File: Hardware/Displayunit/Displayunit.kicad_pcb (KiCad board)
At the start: 2 copper layers, 99 parts, among them IC1 TSC2007, IC2 MX25LM51245GXDI00, IC3 IS66WVH8M8BLL-100B1LI_0, J1 USB_B_Micro, J2 8P8C_Shielded, J3 54104-4031, J4 Conn_ARM_JTAG_SWD_20, J5 52271-0679, J6 Conn_02x06_Odd_Even, Q1 2N7002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

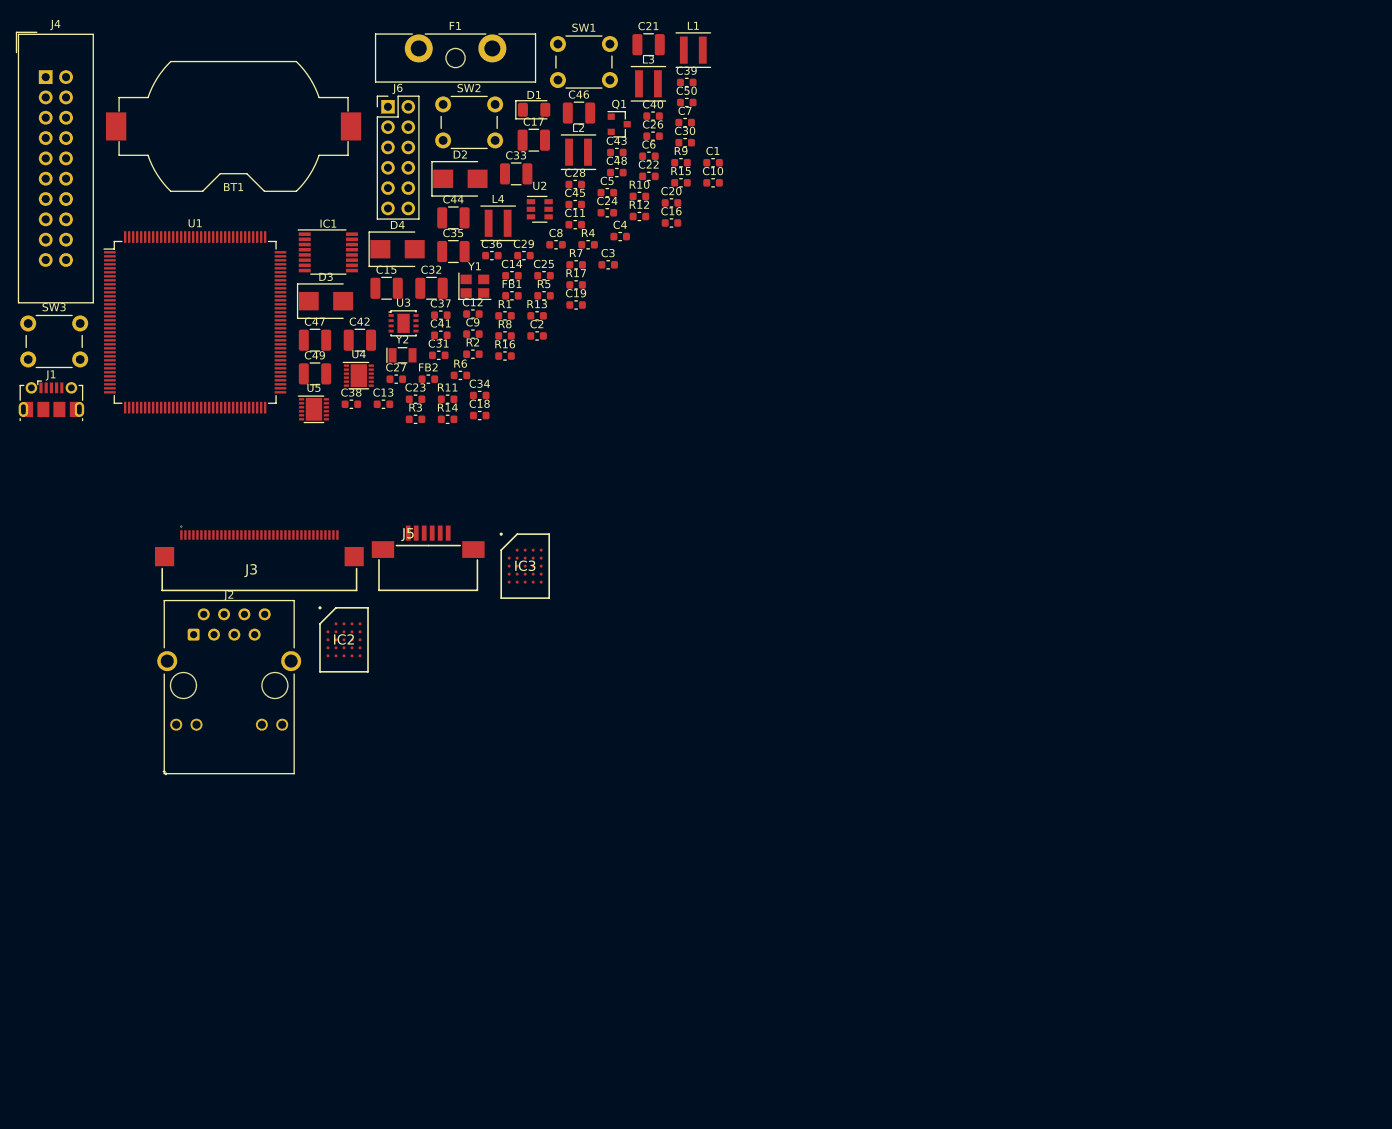
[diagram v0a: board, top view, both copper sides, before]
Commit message: Display Board kleinere Schaltplan Anpassung , Board Design an New Heaven Display angepasst, Platzierung zu 95 % abgeschlossen
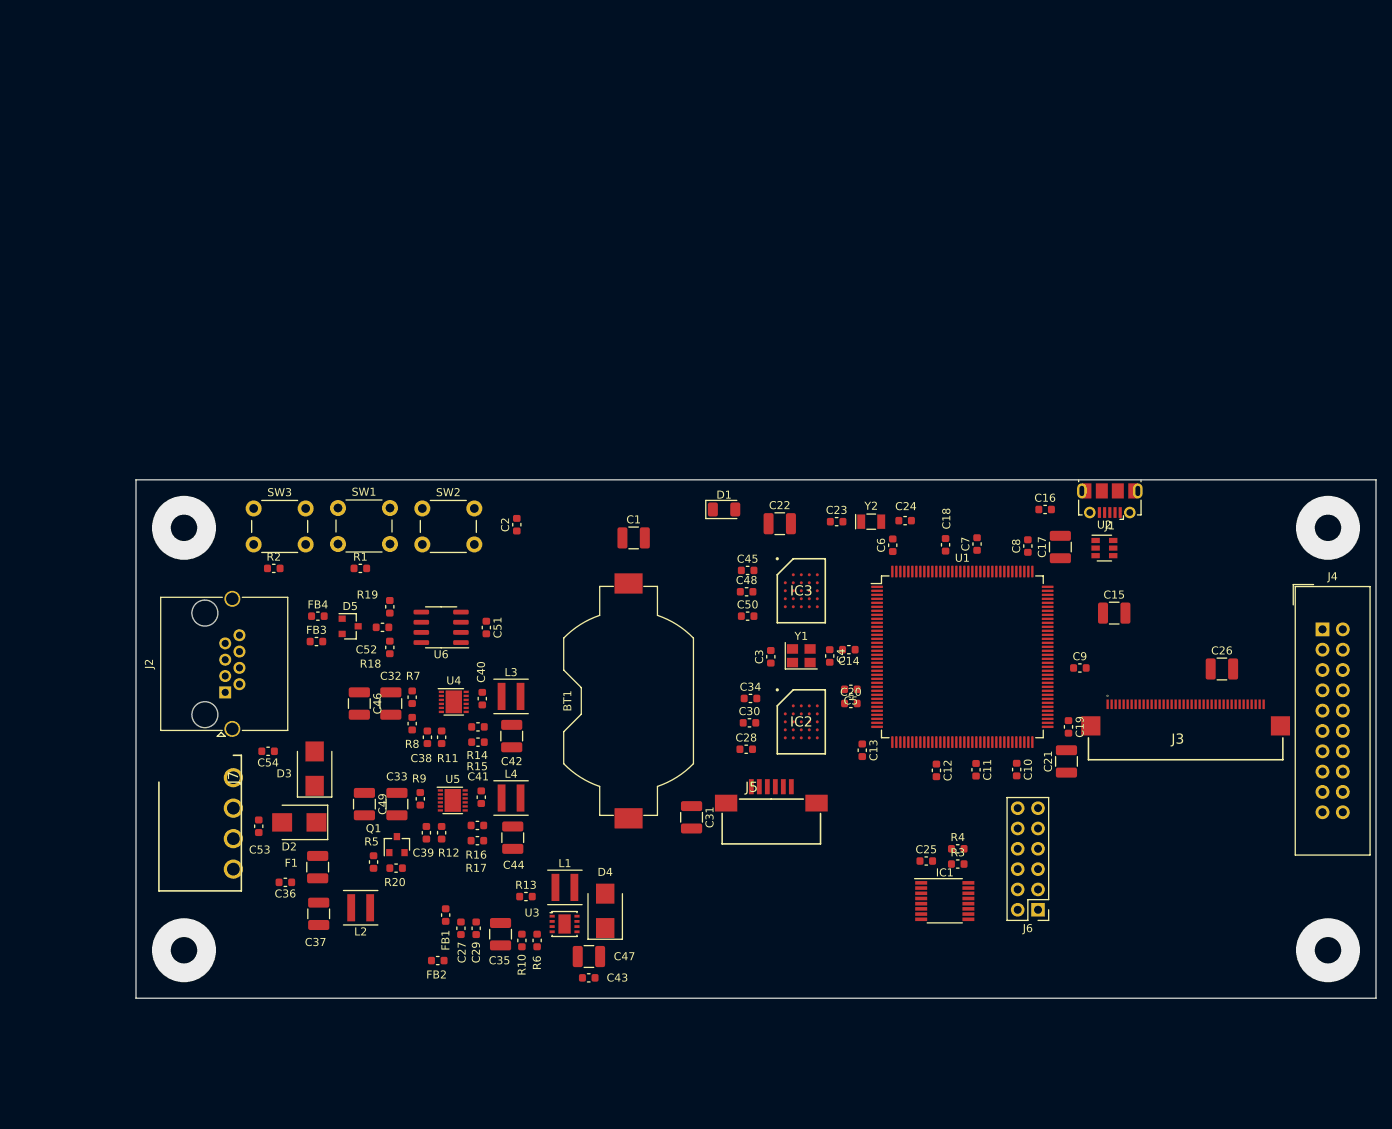
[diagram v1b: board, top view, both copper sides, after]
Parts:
- added C51: 100n, Capacitor_SMD:C_0603_1608Metric, F.Cu at (105.8, 67.5)
- added C52: 5n6, Capacitor_SMD:C_0603_1608Metric, F.Cu at (92.8, 67.4)
- added C53: 100n, Capacitor_SMD:C_0603_1608Metric, F.Cu at (77.3, 92.3)
- added C54: 100n, Capacitor_SMD:C_0603_1608Metric, F.Cu at (78.5, 82.9)
- added D5: NUP2105L, Package_TO_SOT_SMD:SOT-23, F.Cu at (88.8, 67.3)
- added FB3: 100R, Inductor_SMD:L_0603_1608Metric, F.Cu at (84.6, 69.2)
- added FB4: 100R, Inductor_SMD:L_0603_1608Metric, F.Cu at (84.7, 66.0)
- added J7: 734-264, WAGO:SHDR4W120P0X381_1X4_1640X1030X850P, F.Cu at (74.2, 86.2)
- added R18: 60R, Resistor_SMD:R_0603_1608Metric, F.Cu at (93.7, 70.0)
- added R19: 60R, Resistor_SMD:R_0603_1608Metric, F.Cu at (93.7, 64.9)
- added R20: 100k, Resistor_SMD:R_0603_1608Metric, F.Cu at (94.5, 97.5)
- added U6: SN65HVD231, Package_SO:SOIC-8_3.9x4.9mm_P1.27mm, F.Cu at (100.1, 67.4)
- C1, C22, C26, C31, C37: footprint Capacitor_SMD:C_0603_1608Metric -> Capacitor_SMD:C_1210_3225Metric
- D2, D3, D4: value B345BE-13 -> B250
- F1: value KFZ 5A -> PFUF.150.2 30V 1.5A; footprint Fuse:Fuseholder_Blade_ATO_Littelfuse_Pudenz_2_Pin -> Fuse:Fuse_1210_3225Metric
- J2: footprint Connector_RJ:RJ45_Hanrun_HR911105A -> Connector_RJ:RJ45_Amphenol_RJHSE5380
- moved J4 173.9 mm to (210.3, 67.7)
- moved J1 132.9 mm to (183.7, 51.6), turned to 180 degrees
- moved J6 129.1 mm to (174.8, 102.7), turned to 180 degrees
- moved J3 117.7 mm to (193.2, 77.4)
- moved IC1 111.9 mm to (163.1, 101.7)
- moved L1 105.9 mm to (115.6, 99.9)
- moved U1 104.6 mm to (165.3, 71.1)
- moved C21 103.7 mm to (178.3, 84.2), turned to 90 degrees
- moved C43 103.2 mm to (118.6, 111.3), turned to 180 degrees
- moved F1 103.1 mm to (84.7, 97.4), turned to 90 degrees
- moved C15 99.6 mm to (184.3, 65.7)
- moved C39 99.3 mm to (98.3, 93.1), turned to 270 degrees
- moved L2 98.3 mm to (90.1, 102.5), turned to 180 degrees
- moved C26 97.4 mm to (197.7, 72.6)
- moved Q1 94.2 mm to (94.6, 94.6), turned to 90 degrees
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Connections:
- C17 pad 2: GND1 -> GND
- C18 pad 1: GND1 -> GND
- C19 pad 1: GND1 -> GND
- C20 pad 1: GND1 -> GND
- C21 pad 1: GND1 -> GND
- C25 pad 2: VCC -> +3.3VA
- C26 pad 1: VCC -> +3.3VA
- C31 pad 1: VCC -> +3.3VA
- D2 pad 1: GND -> Net-(D2-Pad1)
- D2 pad 2: Net-(D2-Pad2) -> Net-(C53-Pad1)
- D3 pad 1: GND -> Net-(D2-Pad1)
- D3 pad 2: Net-(D2-Pad2) -> Control+
- D4 pad 1: Net-(D4-Pad1) -> LCD_LED-A
- D4 pad 2: LCD_LED-A -> Net-(D4-Pad2)
- F1 pad 1: Net-(D2-Pad2) -> Net-(C36-Pad1)
- F1 pad 2: Net-(C36-Pad1) -> Net-(D2-Pad1)
- FB1 pad 2: Net-(FB1-Pad2) -> +3.3VA
- IC1 pad 1: VCC -> +3.3VA
- IC1 pad 2: Net-(IC1-Pad2) -> X+
- IC1 pad 3: Net-(IC1-Pad3) -> Y+
- IC1 pad 4: Net-(IC1-Pad4) -> X-
- IC1 pad 5: Net-(IC1-Pad5) -> Y-
- IC2 pad B4: VCCQ -> +3V3
- IC2 pad D1: VCCQ -> +3V3
- IC3 pad B4: VCCQ -> +3V3
- IC3 pad D1: VCCQ -> +3V3
- J2 pad 1: Net-(J2-Pad1) -> Control+
- J2 pad 2: Net-(J2-Pad2) -> Control+
- J2 pad 7: Net-(J2-Pad7) -> GND
- J2 pad 8: Net-(J2-Pad8) -> GND
- J2 pad SH: Net-(J2-PadSH) -> GND
- J3 pad 4: VCC -> +3.3VA
- J5 pad 1: VCC -> +3.3VA
- J5 pad 2: Net-(J5-Pad2) -> GND
- L1 pad 2: Net-(D4-Pad1) -> Net-(D4-Pad2)
- L2 pad 2: Net-(D2-Pad2) -> Net-(C36-Pad1)
- R13 pad 1: +VSW -> +3.3VA
- R3 pad 1: VCC -> +3.3VA
- R4 pad 1: VCC -> +3.3VA
- U2 pad 3: Net-(U2-Pad3) -> USB_D+
- U3 pad 8: Net-(D4-Pad1) -> Net-(D4-Pad2)
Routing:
- net GND: vias 0 -> 1
- net (no net): vias 0 -> 3
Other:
- board outline added: 155 x 64.8 mm

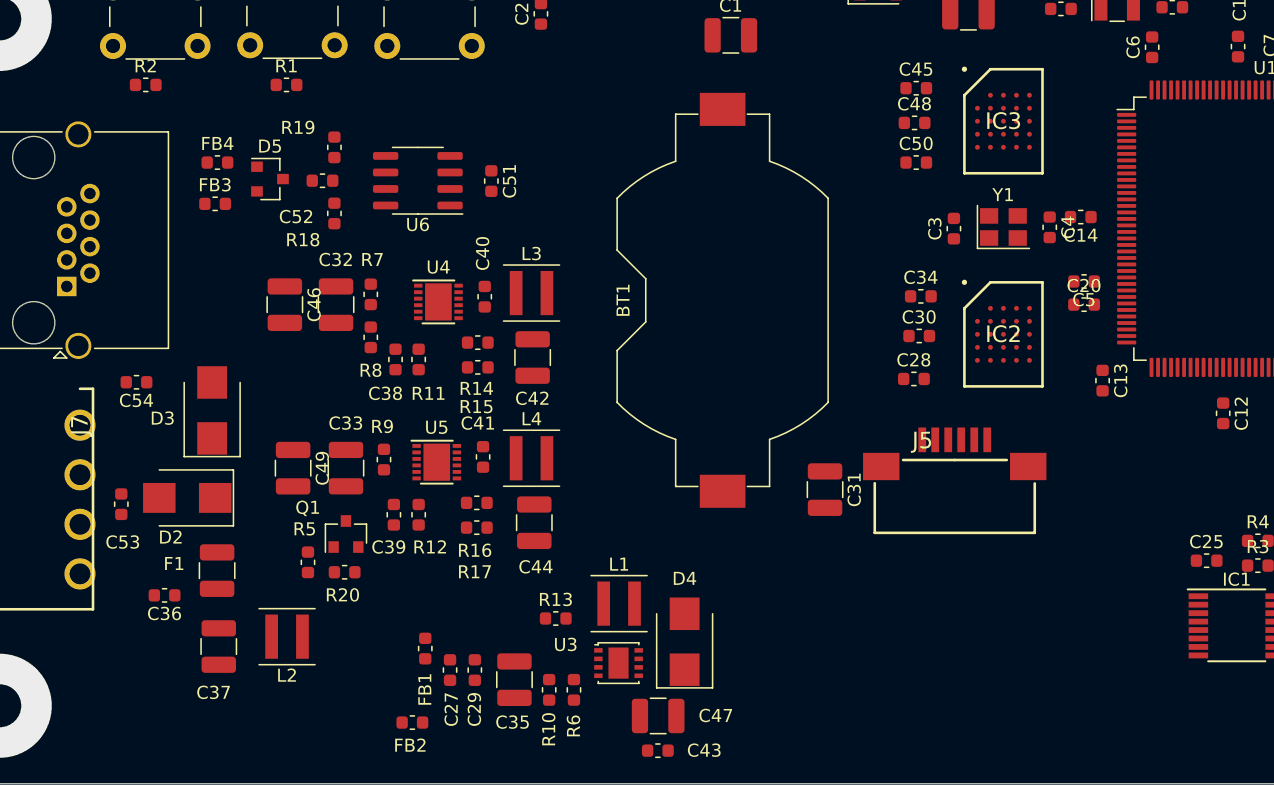
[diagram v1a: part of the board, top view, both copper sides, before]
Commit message: Displayboard: etwas Layout am Powersupply
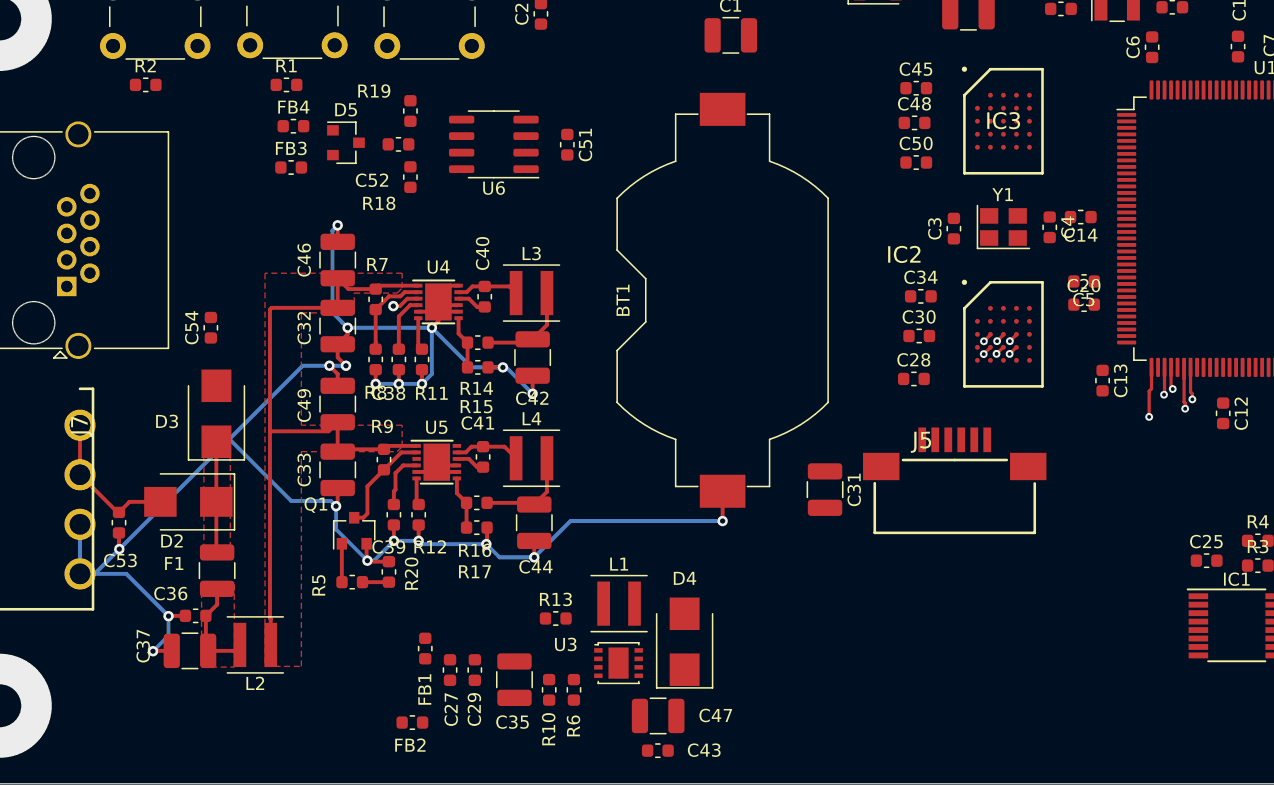
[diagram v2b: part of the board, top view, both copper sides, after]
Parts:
- IC2: value MX25LM51245GXDI00 -> M
- moved C54 7.09 mm to (84.2, 78.7), turned to 90 degrees
- moved C51 6.48 mm to (111.6, 64.7)
- moved FB4 6.48 mm to (90.6, 63.2)
- moved C52 6.48 mm to (98.7, 64.6)
- moved D5 6.48 mm to (94.6, 64.5)
- moved FB3 6.48 mm to (90.4, 66.4)
- moved R18 6.48 mm to (99.6, 67.2)
- moved R19 6.48 mm to (99.6, 62.1)
- moved U6 6.48 mm to (106.0, 64.6)
- moved C49 6.01 mm to (94.0, 84.6), turned to 90 degrees
- moved C46 5.32 mm to (94.0, 73.5), turned to 90 degrees
- moved R5 3.73 mm to (95.1, 98.3), turned to 0 degrees
- moved R20 3.40 mm to (97.9, 97.5), turned to 90 degrees
- moved C36 2.86 mm to (83.1, 100.9)
- moved L2 2.52 mm to (87.6, 103.1)
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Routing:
- net GND: track 0.00 -> 163.8 mm, vias 1 -> 21
- net +BATT: track 0.00 -> 54.0 mm
- net OctoSPI_P1_NCS: track 0.00 -> 21.4 mm, vias 0 -> 2
- net OctoSPI_P1_IO1: track 0.00 -> 21.2 mm, vias 0 -> 2
- net OctoSPI_P1_IO0: track 0.00 -> 20.2 mm, vias 0 -> 2
- net OctoSPI_P1_IO2: track 0.00 -> 17.4 mm, vias 0 -> 2
- net OctoSPI_P1_IO3: track 0.00 -> 16.6 mm, vias 0 -> 2
- net Net-(C53-Pad1): track 0.00 -> 11.5 mm
- net Net-(D2-Pad1): track 0.00 -> 8.54 mm
- net Net-(Q1-Pad3): track 0.00 -> 8.15 mm
- net Net-(C36-Pad1): track 0.00 -> 7.83 mm
- net +3.3VA: track 0.00 -> 7.64 mm
- net +3V3: track 0.00 -> 7.55 mm
- net Net-(R7-Pad2): track 0.00 -> 6.87 mm
- net Net-(C41-Pad1): track 0.00 -> 5.10 mm
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- added copper zone on F.Cu, net +BATT
- added copper zone on F.Cu, net Net-(C36-Pad1)
- added copper zone on F.Cu, net Net-(D2-Pad1)
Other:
- copper layers 2 -> 4

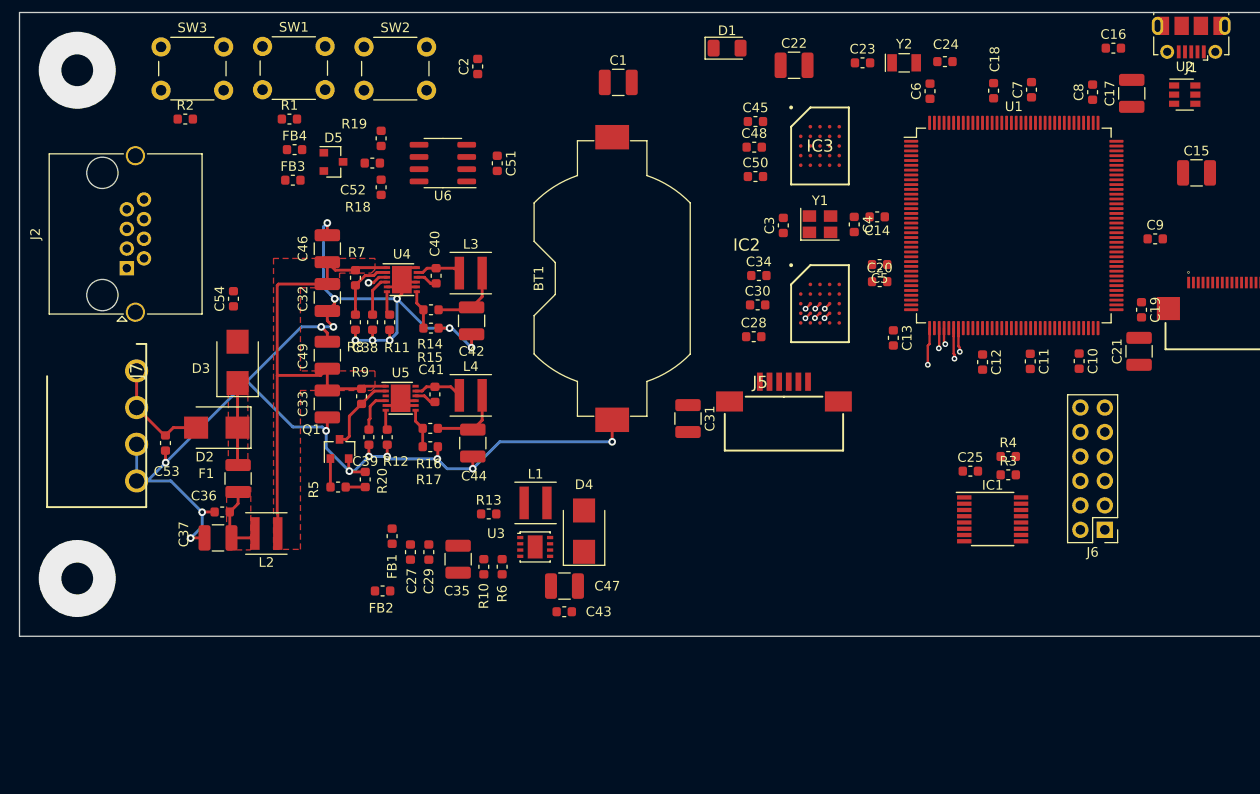
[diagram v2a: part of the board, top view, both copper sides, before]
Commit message: Displayunit: Zweite Controlbus Buchse hinzugefügt.
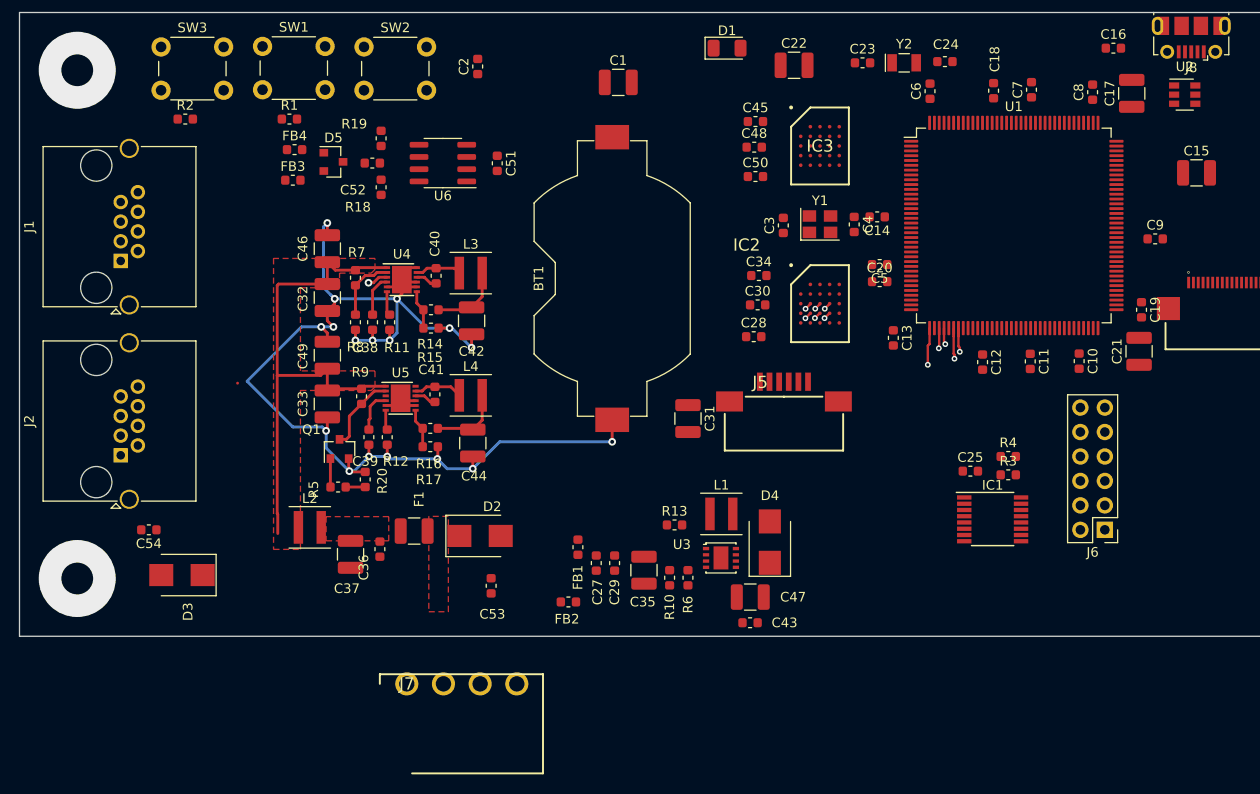
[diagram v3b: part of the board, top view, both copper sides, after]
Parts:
- added J2: 8P8C_Shielded, Connector_RJ:RJ45_Amphenol_RJHSE5380, F.Cu at (72.5, 95.0)
- IC2: value M -> MX25LM51245GXDI00
- moved J7 43.0 mm to (102.2, 118.7), turned to 0 degrees
- moved C53 36.9 mm to (111.0, 108.6)
- moved D2 29.6 mm to (109.8, 103.4), turned to 0 degrees
- moved C54 25.6 mm to (75.4, 102.7), turned to 180 degrees
- moved D3 22.8 mm to (78.9, 107.4), turned to 180 degrees
- moved C47 19.3 mm to (137.9, 109.7)
- moved C27 19.3 mm to (121.9, 106.2)
- moved C29 19.3 mm to (123.8, 106.2)
- moved C35 19.3 mm to (126.9, 106.9)
- moved C43 19.3 mm to (137.9, 112.4)
- moved D4 19.3 mm to (140.0, 104.0)
- moved FB1 19.3 mm to (120.0, 104.5)
- moved FB2 19.3 mm to (119.0, 110.2)
- moved L1 19.3 mm to (134.9, 101.1)
- moved R13 19.3 mm to (130.0, 102.2)
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- renumbered J2 to J1, J1 to J8
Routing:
- net GND: track 163.8 -> 128.8 mm, vias 21 -> 18
- net Net-(C53-Pad1): track 11.5 -> 0.00 mm
- net Net-(D2-Pad1): track 8.54 -> 0.01 mm
- net Net-(C36-Pad1): track 7.83 -> 0.00 mm
